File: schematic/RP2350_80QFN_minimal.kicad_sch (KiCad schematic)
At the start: 39 parts, among them J4 SM03B-SRSS-TB, SW1 SW_Push, SW2 SW_Push, U1 RP2350_80QFN, U3 W25Q128JVS, Y1 ABM8-272-T3

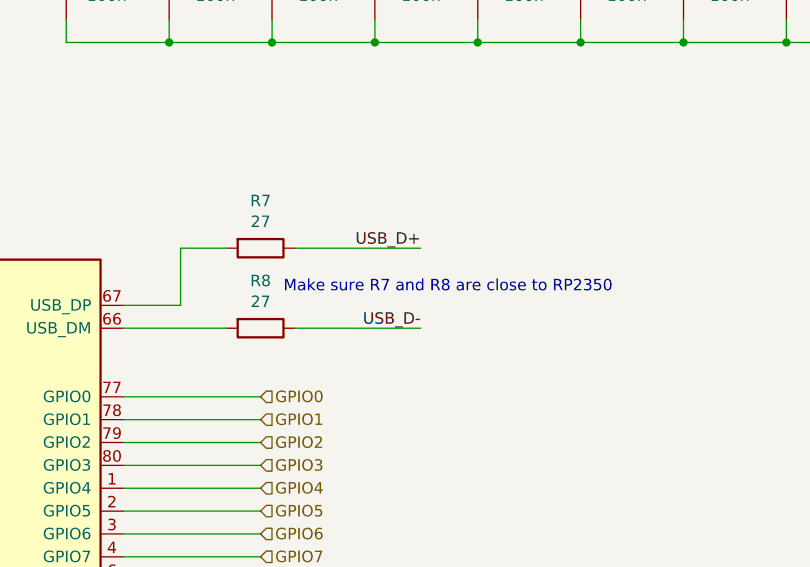
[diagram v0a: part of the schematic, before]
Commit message: fix: the D+ and D- lines were unedited from the official rp2350B example schematic
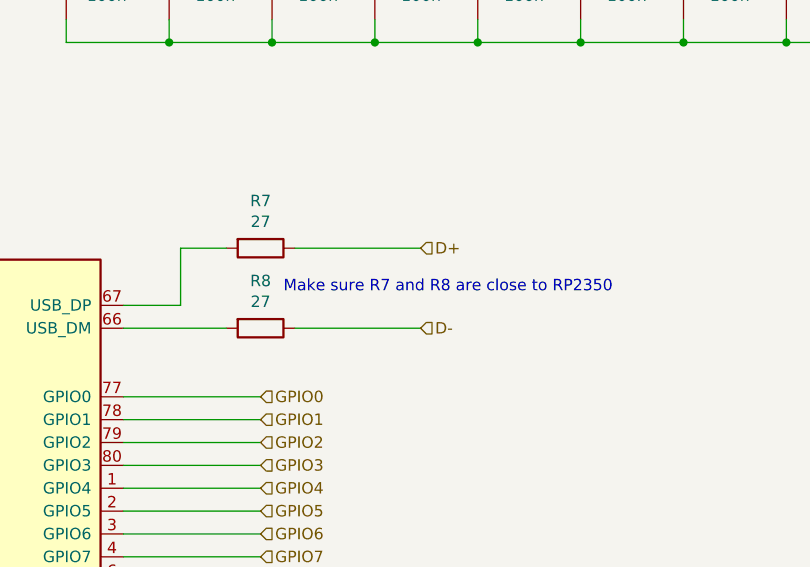
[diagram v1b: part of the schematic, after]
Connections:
- net USB_D+ renamed D+
- net USB_D- renamed D-
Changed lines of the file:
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@@
-		)
-	)
-	(label "USB_D+"
-		(at 267.97 95.25 180)
-		(effects
-			(font
-				(size 1.27 1.27)
-			)
-			(justify right bottom)
 		)
 	)
@@
 		)
 	)
-	(label "USB_D-"
-		(at 267.97 104.14 180)
-		(effects
-			(font
-				(size 1.27 1.27)
-			)
-			(justify right bottom)
-		)
-	)
 	(label "VREG_AVDD"
 		(at 154.305 90.17 0)
@@
 		)
 	)
+	(hierarchical_label "D-"
+		(shape input)
+		(at 267.97 104.14 0)
+		(effects
+			(font
+				(size 1.27 1.27)
+			)
+			(justify left)
+		)
+	)
 	(hierarchical_label "GPIO0"
 		(shape input)
@@
 		(effects
 			(font
+				(size 1.27 1.27)
+			)
+			(justify left)
+		)
+	)
+	(hierarchical_label "D+"
+		(shape input)
+		(at 267.97 95.25 0)
+		(effects
+			(font
